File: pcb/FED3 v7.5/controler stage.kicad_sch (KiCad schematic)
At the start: 25 parts, among them IC4 RTC PCF8523T, J1 Conn_02x03_Odd_Even, SW2 SPST_TACT-KMR2, U1 ATSAMD21G18A, U4 Adafruit LCD Screen, X1 ClockXtal, X2 uXtal, X4 microsd

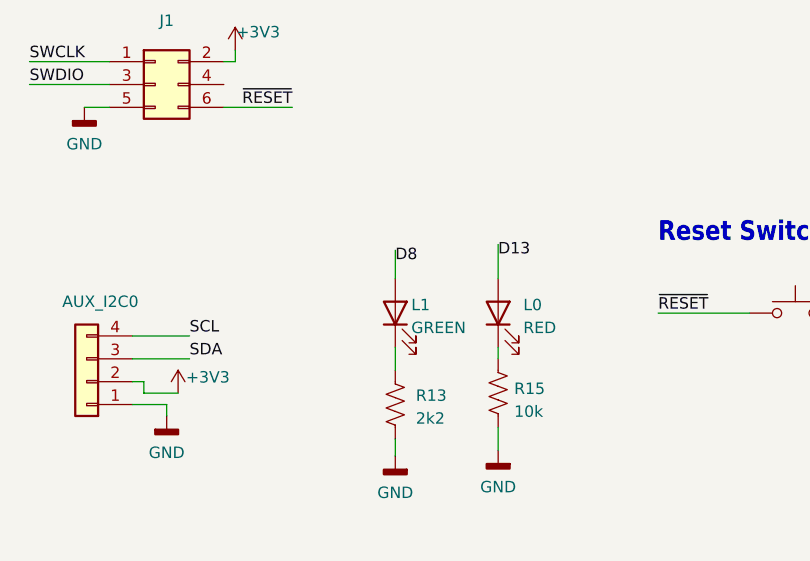
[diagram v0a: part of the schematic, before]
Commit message: FED3 v.7.5 - 1ºs ficheiros de progução
- adicionada header para opção VTherm = Vbat
- optimização para BOM: variedade-vs-quantidade
- optimização de power-planes
- gerados ficheiros produção para 1ª avaliação; há lá erros reconhecidos
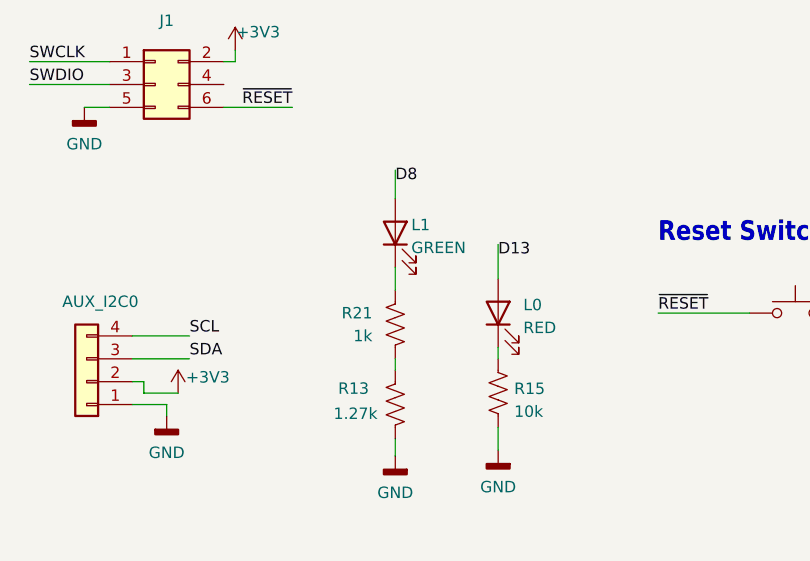
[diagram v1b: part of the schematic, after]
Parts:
- added R21: 1k, Resistor_SMD:R_0402_1005Metric, symbol Device:R_US
- R13: value 2k2 -> 1.27k; MPN ERJ-2RKF2201X -> CRCW04021K27FKED; OEPSPN OEPS020174 -> OEPS020190
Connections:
- net at R13.1: now also R21.1; no longer L1.1 (K)
- new net: L1.1 (K), R21.2
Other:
- moved on the sheet: L1
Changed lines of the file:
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@@
 	(wire
 		(pts
+			(xy 105.41 166.37) (xy 105.41 167.64)
+		)
+		(stroke
+			(width 0)
+			(type default)
+		)
+	)
+	(wire
+		(pts
 			(xy 207.01 133.35) (xy 210.185 133.35)
 		)
@@
 	(wire
 		(pts
-			(xy 105.41 154.305) (xy 105.41 157.48)
+			(xy 105.41 145.415) (xy 105.41 148.59)
 		)
 		(stroke
@@
 	(wire
 		(pts
-			(xy 105.41 165.1) (xy 105.41 167.64)
+			(xy 105.41 156.21) (xy 105.41 158.75)
 		)
 		(stroke
@@
 	)
 	(label "D8"
-		(at 105.41 154.305 0)
+		(at 105.41 145.415 0)
 		(effects
 			(font
@@
 	)
 	(symbol
+		(lib_id "Device:R_US")
+		(at 105.41 171.45 0)
+		(mirror y)
+		(unit 1)
+		(exclude_from_sim no)
+		(in_bom yes)
+		(on_board yes)
+		(dnp no)
+		(property "Reference" "R13"
+			(at 99.06 169.672 0)
+			(effects
+				(font
+					(size 1.27 1.27)
+				)
+				(justify right)
+			)
+		)
+		(property "Value" "1.27k"
+			(at 98.552 172.466 0)
+			(effects
+				(font
+					(size 1.27 1.27)
+				)
+				(justify right)
+			)
+		)
+		(property "Footprint" "Resistor_SMD:R_0402_1005Metric"
+			(at 105.41 171.45 0)
+			(effects
+				(font
+					(size 1.27 1.27)
+				)
+				(hide yes)
+			)
+		)
+		(property "Datasheet" ""
+			(at 105.41 171.45 0)
+			(effects
+				(font
+					(size 1.27 1.27)
+				)
+				(hide yes)
+			)
+		)
+		(property "Description" "SMD 0402 1.27kΩ ±1% 0.100W"
+			(at 105.41 171.45 0)
+			(effects
+				(font
+					(size 1.27 1.27)
+				)
+				(hide yes)
+			)
+		)
+		(property "OEPSPN" "OEPS020190"
+			(at 105.41 171.45 0)
+			(effects
+				(font
+					(size 1.27 1.27)
+				)
+				(hide yes)
+			)
+		)
+		(property "MPN" "CRCW04021K27FKED"
+			(at 105.41 171.45 0)
+			(effects
+				(font
+					(size 1.27 1.27)
+				)
+				(hide yes)
+			)
+		)
+		(pin "1"
+		)
+		(pin "2"
+		)
+		(instances
+			(project "FED3"
+				(path "/2ba63f12-2fcd-4471-9636-2762cde37de8/f4901940-5078-48a6-adaa-a0748712c93b"
+					(reference "R13")
+					(unit 1)
+				)
+			)
+		)
+	)
+	(symbol
 		(lib_id "Device:C_Small")
 		(at 135.89 29.21 180)
@@
 	(symbol
 		(lib_id "Device:LED")
-		(at 105.41 161.29 90)
+		(at 105.41 152.4 90)
 		(unit 1)
 		(exclude_from_sim no)
@@
 		(dnp no)
 		(property "Reference" "L1"
-			(at 107.188 159.639 90)
+			(at 107.188 150.749 90)
 			(effects
 				(font
@@
 		)
 		(property "Value" "GREEN"
-			(at 107.188 162.179 90)
+			(at 107.188 153.289 90)
 			(effects
 				(font
@@
 		)
 		(property "Footprint" "LED_SMD:LED_0603_1608Metric"
-			(at 105.41 161.29 0)
+			(at 105.41 152.4 0)
 			(effects
 				(font
@@
 		)
 		(property "Datasheet" ""
-			(at 105.41 161.29 0)
+			(at 105.41 152.4 0)
 			(effects
 				(font
@@
 		)
 		(property "Description" "LED 0603 Green 570nm 20mA"
-			(at 105.41 161.29 0)
+			(at 105.41 152.4 0)
 			(effects
 				(font
@@
 		)
 		(property "OEPSPN" "OEPS030005"
-			(at 105.41 161.29 0)
+			(at 105.41 152.4 0)
 			(effects
 				(font
@@
 		)
 		(property "MPN" "150060VS75000"
-			(at 105.41 161.29 0)
+			(at 105.41 152.4 0)
 			(effects
 				(font
@@
 	)
 	(symbol
+		(lib_id "Device:R_US")
+		(at 105.41 162.56 0)
+		(mirror x)
+		(unit 1)
+		(exclude_from_sim no)
+		(in_bom yes)
+		(on_board yes)
+		(dnp no)
+		(fields_autoplaced yes)
+		(property "Reference" "R21"
+			(at 102.87 161.2899 0)
+			(effects
+				(font
+					(size 1.27 1.27)
+				)
+				(justify right)
+			)
+		)
+		(property "Value" "1k"
+			(at 102.87 163.8299 0)
+			(effects
+				(font
+					(size 1.27 1.27)
+				)
+				(justify right)
+			)
+		)
+		(property "Footprint" "Resistor_SMD:R_0402_1005Metric"
+			(at 105.41 162.56 0)
+			(effects
+				(font
+					(size 1.27 1.27)
+				)
+				(hide yes)
+			)
+		)
+		(property "Datasheet" ""
+			(at 105.41 162.56 0)
+			(effects
+				(font
+					(size 1.27 1.27)
+				)
+				(hide yes)
+			)
+		)
+		(property "Description" "SMD 0402 1kΩ ±1% 0.100W"
+			(at 105.41 162.56 0)
+			(effects
+				(font
+					(size 1.27 1.27)
+				)
+				(hide yes)
+			)
+		)
+		(property "OEPSPN" "OEPS020006"
+			(at 105.41 162.56 0)
+			(effects
+				(font
+					(size 1.27 1.27)
+				)
+				(hide yes)
+			)
+		)
+		(property "MPN" "ERJ-2RKF1001X"
+			(at 105.41 162.56 0)
+			(effects
+				(font
+					(size 1.27 1.27)
+				)
+				(hide yes)
+			)
+		)
+		(pin "2"
+		)
+		(pin "1"
+		)
+		(instances
+			(project "FED3"
+				(path "/2ba63f12-2fcd-4471-9636-2762cde37de8/f4901940-5078-48a6-adaa-a0748712c93b"
+					(reference "R21")
+					(unit 1)
+				)
+			)
+		)
+	)
+	(symbol
 		(lib_id "Connector_Generic:Conn_01x04")
 		(at 71.12 168.91 180)
@@
 					(unit 1)
 				)
-			)
-		)
-	)
-	(symbol
-		(lib_id "Device:R_US")
-		(at 105.41 171.45 0)
-		(unit 1)
-		(exclude_from_sim no)
-		(in_bom yes)
-		(on_board yes)
-		(dnp no)
-		(property "Reference" "R13"
-			(at 107.696 171.196 0)
-			(effects
-				(font
-					(size 1.27 1.27)
-				)
-				(justify left bottom)
-			)
-		)
-		(property "Value" "2k2"
-			(at 107.696 173.736 0)
-			(effects
-				(font
-					(size 1.27 1.27)
-					(thickness 0.127)
-				)
-				(justify left bottom)
-			)
-		)
-		(property "Footprint" "Resistor_SMD:R_0402_1005Metric"
-			(at 105.41 171.45 0)
-			(effects
-				(font
-					(size 1.27 1.27)
-				)
-				(hide yes)
-			)
-		)
-		(property "Datasheet" ""
-			(at 105.41 171.45 0)
-			(effects
-				(font
-					(size 1.27 1.27)
-				)
-				(hide yes)
-			)
-		)
-		(property "Description" "SMD 0402 2.2kΩ ±1% 0.100W"
-			(at 105.41 171.45 0)
-			(effects
-				(font
-					(size 1.27 1.27)
-				)
-				(hide yes)
-			)
-		)
-		(property "OEPSPN" "OEPS020174"
-			(at 105.41 171.45 0)
-			(effects
-				(font
-					(size 1.27 1.27)
-				)
-				(hide yes)
-			)
-		)
-		(property "MPN" "ERJ-2RKF2201X"
-			(at 105.41 171.45 0)
-			(effects
-				(font
-					(size 1.27 1.27)
-				)
-				(hide yes)
-			)
-		)
-		(pin "1"
-		)
-		(pin "2"
-		)
-		(instances
-			(project "FED3_v7.3"
-				(path "/2ba63f12-2fcd-4471-9636-2762cde37de8/f4901940-5078-48a6-adaa-a0748712c93b"
-					(reference "R13")
-					(unit 1)
-				)

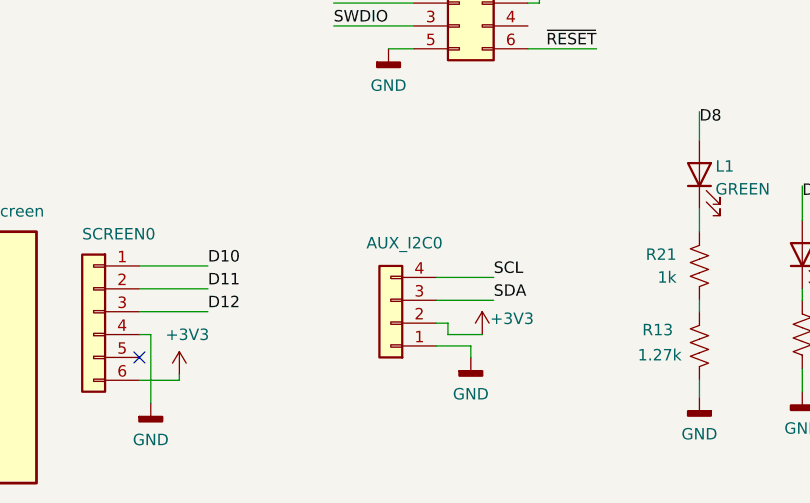
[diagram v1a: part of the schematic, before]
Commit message: FED3 v.7.5 - 2ºs ficheiros produção
- corrigidas posições de silks de alguns componentes
- modificados Denominators de alguns componentes
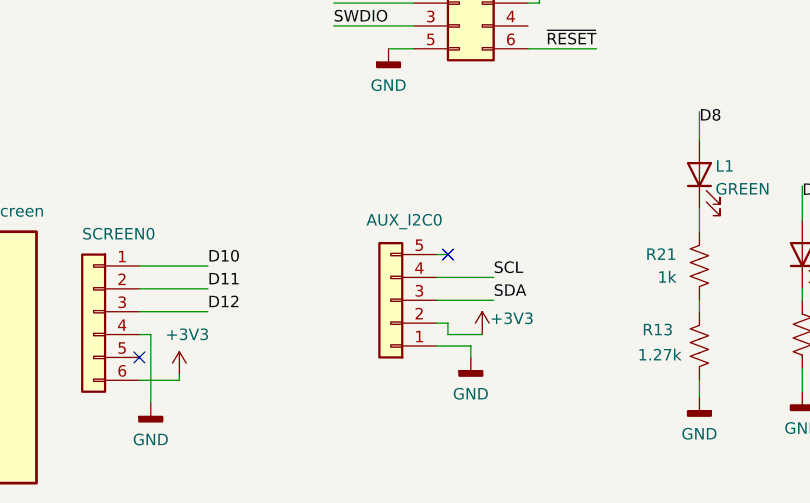
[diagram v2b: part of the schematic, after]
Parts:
- AUX_I2C0: symbol Connector_Generic:Conn_01x04 -> Connector_Generic:Conn_01x05
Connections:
- no-connect marks 14 -> 15
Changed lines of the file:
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@@
 	)
 	(no_connect
+		(at 77.47 161.29)
+	)
+	(no_connect
 		(at 120.65 67.31)
 	)
@@
 	(wire
 		(pts
+			(xy 77.47 161.29) (xy 76.2 161.29)
+		)
+		(stroke
+			(width 0)
+			(type default)
+		)
+	)
+	(wire
+		(pts
 			(xy 207.01 146.05) (xy 219.71 146.05)
 		)
@@
 	)
 	(symbol
-		(lib_id "Connector_Generic:Conn_01x04")
-		(at 71.12 168.91 180)
+		(lib_id "Connector_Generic:Conn_01x05")
+		(at 71.12 166.37 180)
 		(unit 1)
 		(exclude_from_sim no)
@@
 		(dnp no)
 		(property "Reference" "AUX_I2C0"
-			(at 72.644 160.02 0)
+			(at 72.644 157.48 0)
 			(effects
 				(font
@@
 		)
 		(property "Value" "Qwiic"
-			(at 77.47 161.29 0)
+			(at 77.47 158.75 0)
 			(effects
 				(font
@@
 		)
 		(property "Footprint" "Connector_JST:JST_SH_BM04B-SRSS-TB_1x04-1MP_P1.00mm_Vertical"
-			(at 71.12 168.91 0)
+			(at 71.12 166.37 0)
 			(effects
 				(font
@@
 		)
 		(property "Datasheet" "~"
-			(at 71.12 168.91 0)
+			(at 71.12 166.37 0)
 			(effects
 				(font
@@
 			)
 		)
-		(property "Description" "Generic connector, single row, 01x04, script generated (kicad-library-utils/schlib/autogen/connector/)"
-			(at 71.12 168.91 0)
+		(property "Description" "Generic connector, single row, 01x05, script generated (kicad-library-utils/schlib/autogen/connector/)"
+			(at 71.12 166.37 0)
 			(effects
 				(font
@@
 		)
 		(property "OEPSPN" "OEPS070125"
-			(at 71.12 168.91 0)
+			(at 71.12 166.37 0)
 			(effects
 				(font
@@
 		)
 		(property "MPN" "BM04B-SRSS-TB(LF)(SN)"
-			(at 71.12 168.91 0)
+			(at 71.12 166.37 0)
 			(effects
 				(font
@@
 		(pin "1"
 		)
+		(pin "5"
+		)
 		(instances
